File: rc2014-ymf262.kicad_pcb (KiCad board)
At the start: 2 copper layers, 100 x 50 mm, 19 parts, among them CON1 SJ1-3523N, P1 RC2014 BUS, U1 74HCT688, U2 YM3812, U3 YM3014B, U4 LM358, X1 3.579545MHz

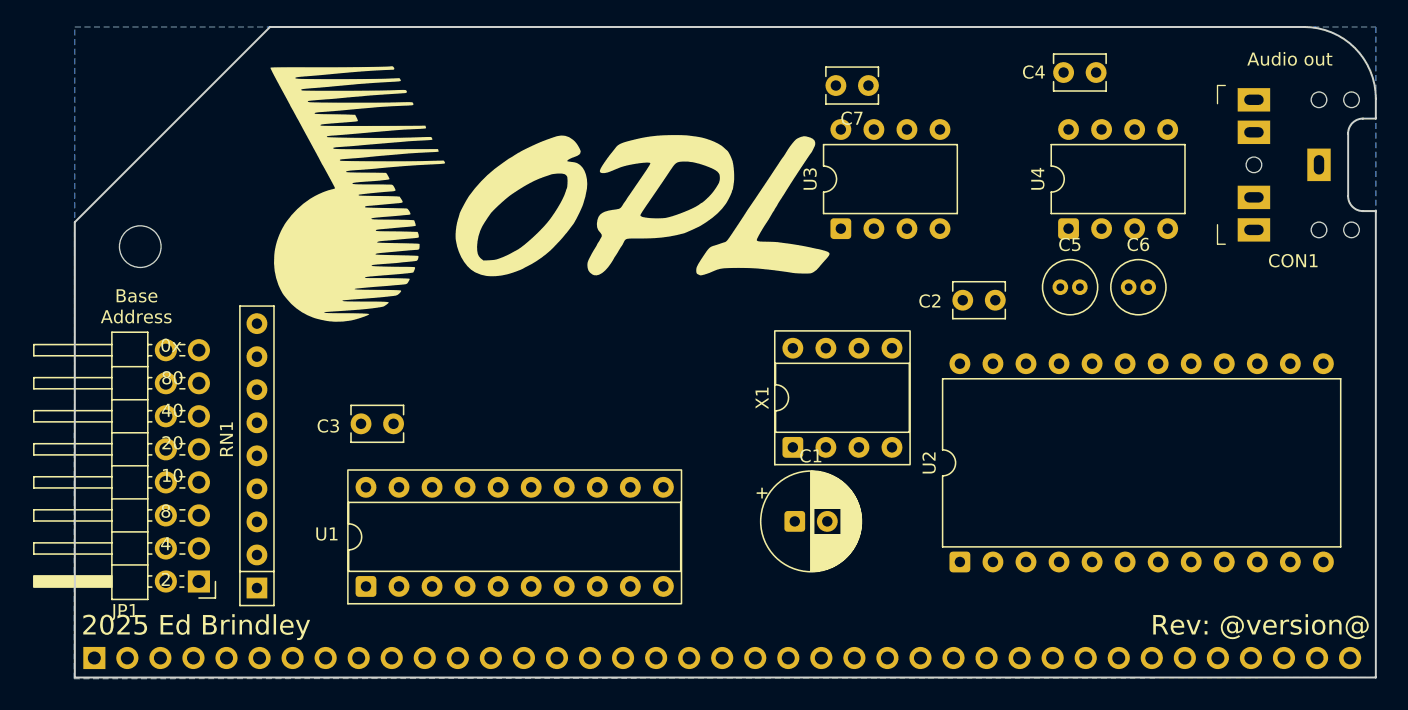
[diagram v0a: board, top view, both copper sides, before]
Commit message: move to use mostly SMD
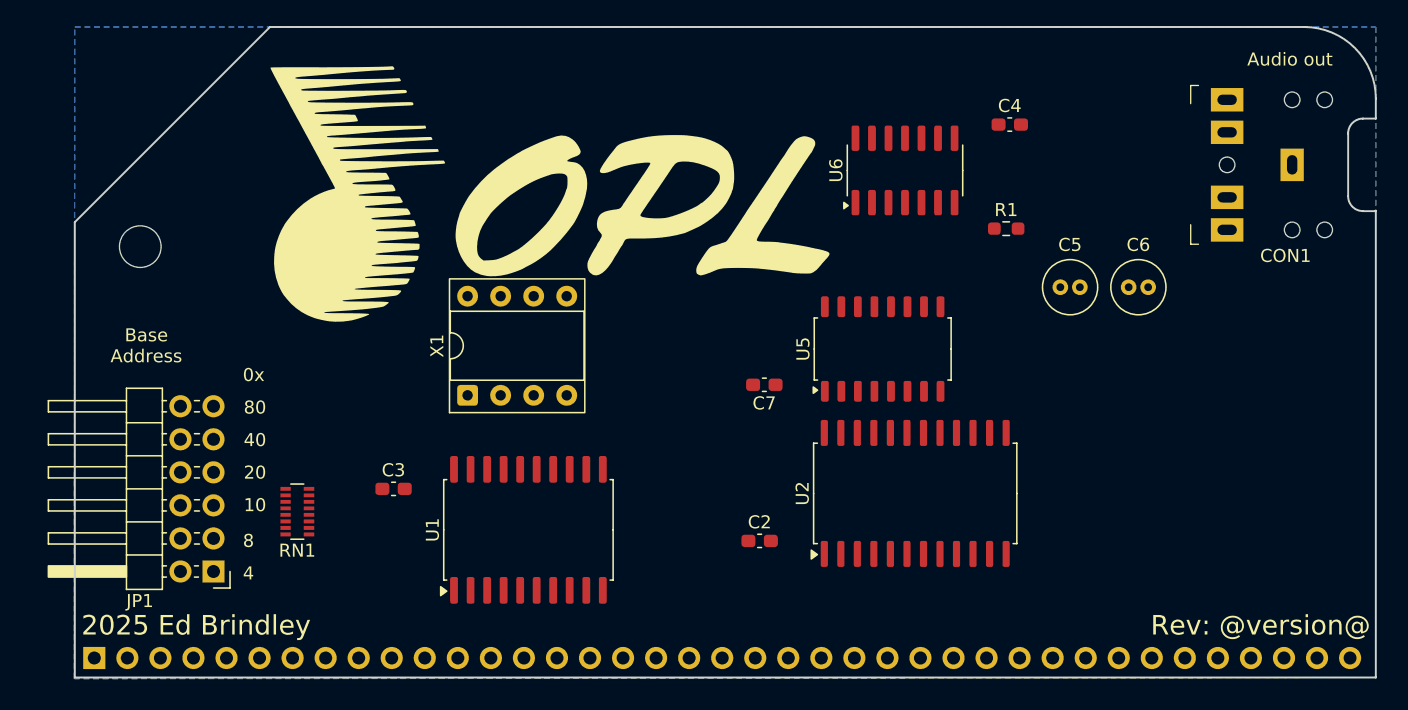
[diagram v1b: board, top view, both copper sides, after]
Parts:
- removed C1: 4.7uF, Capacitor_THT:CP_Radial_D7.5mm_P2.50mm
- removed U3: YM3014B, Package_DIP:DIP-8_W7.62mm
- removed U4: LM358, Package_DIP:DIP-8_W7.62mm
- added R1: R, Resistor_SMD:R_0603_1608Metric_Pad0.98x0.95mm_HandSolder, F.Cu at (132.1, 130.0)
- added U5: YAC512, Package_SO:SOP-16_4.55x10.3mm_P1.27mm, F.Cu at (122.6, 139.2)
- added U6: TL074, Package_SO:SOIC-14_3.9x8.7mm_P1.27mm, F.Cu at (124.3, 125.5)
- C2, C3, C4, C7: footprint Capacitor_THT:C_Disc_D3.8mm_W2.6mm_P2.50mm -> Capacitor_SMD:C_0603_1608Metric_Pad1.08x0.95mm_HandSolder
- JP1: footprint Connector_PinHeader_2.54mm:PinHeader_2x08_P2.54mm_Horizontal -> Connector_PinHeader_2.54mm:PinHeader_2x06_P2.54mm_Horizontal
- RN1: footprint Resistor_THT:R_Array_SIP9 -> Resistor_SMD:R_Array_Convex_8x0602
- U1: footprint Package_DIP:DIP-20_W7.62mm_Socket -> Package_SO:SOIC-20W_7.5x12.8mm_P1.27mm
- U2: value YM3812 -> YMF262; footprint Package_DIP:DIP-24_W15.24mm -> Package_SO:SOP-24_7.5x15.4mm_P1.27mm
- X1: value 3.579545MHz -> 14.318MHz
- moved X1 25.3 mm to (90.7, 142.8)
- moved C7 24.4 mm to (113.5, 142.0)
- moved C2 24.2 mm to (113.1, 154.0)
- moved U1 13.2 mm to (95.4, 153.2)
- moved RN1 6.64 mm to (77.6, 151.8), turned to 180 degrees
- moved U2 6.29 mm to (125.1, 150.3)
- moved C4 5.75 mm to (132.4, 122.0)
- moved C3 5.59 mm to (85.0, 150.0)
- moved CON1 2.06 mm to (149.1, 125.1)
- moved JP1 1.36 mm to (71.2, 156.3)
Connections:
- CON1 pad R: Net-(U4A--) -> /R
- CON1 pad RN: Net-(U4A--) -> /R
- CON1 pad T: Net-(U4A--) -> /L
- CON1 pad TN: Net-(U4A--) -> /L
- RN1 pad 8: Net-(JP1-Pin_14) -> (no net)
- RN1 pad 9: Net-(JP1-Pin_16) -> (no net)
- U1 pad 15: /A1 -> GND
- U1 pad 16: Net-(JP1-Pin_14) -> GND
- U2 pad 19: unconnected-(U2-NC-Pad19) -> /SMPBD
- U2 pad 20: /LOAD -> /SMPAC
- U2 pad 21: /SD -> /DOAB
- U2 pad 5: /~{WR} -> /A1
- U2 pad 6: /~{RD} -> /~{WR}
- U2 pad 7: /~{CS} -> /~{RD}
- U2 pad 8: unconnected-(U2-NC-Pad8) -> /~{CS}
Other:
- board text removed: "2"

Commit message: use custom oscillator footprint
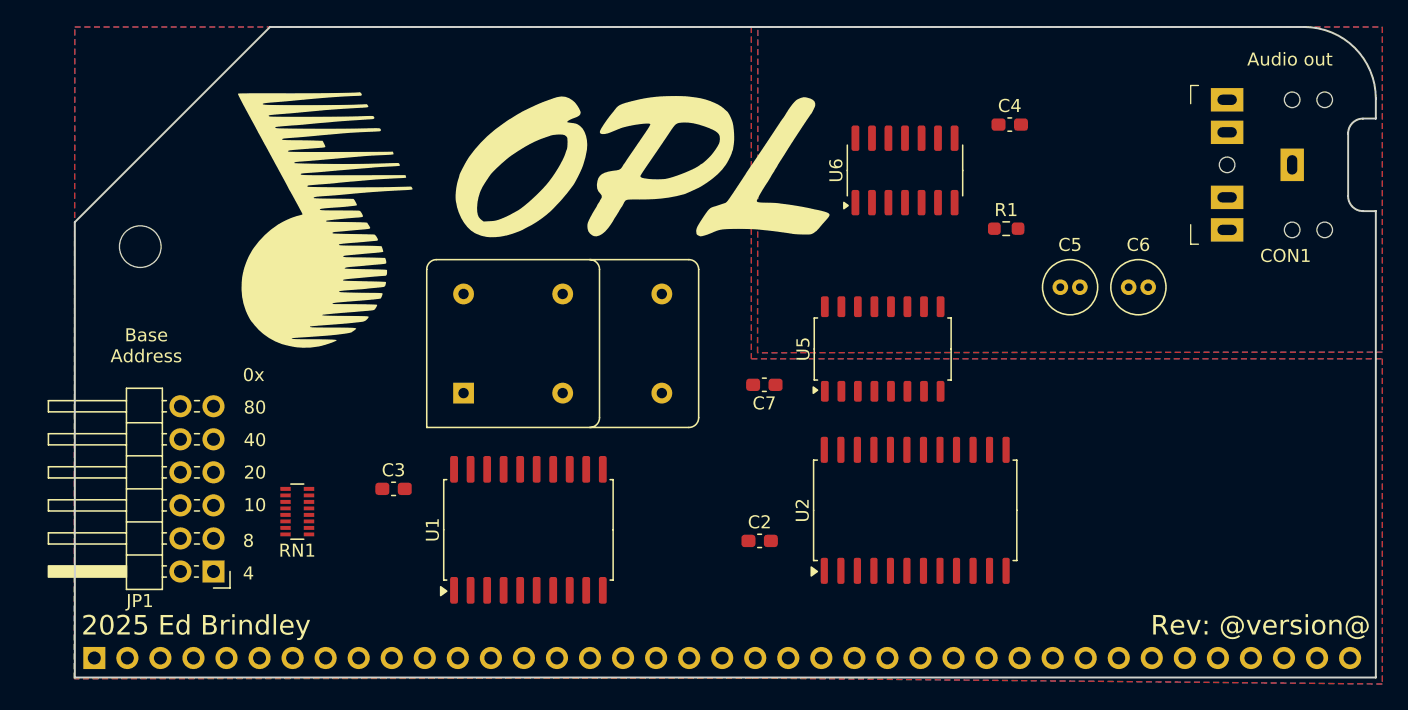
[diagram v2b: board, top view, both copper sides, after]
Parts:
- X1: footprint Package_DIP:DIP-8_W7.62mm_Socket -> electrified:Oscillator_DIP-8-14
- moved X1 8.24 mm to (98.0, 139.0), turned to 0 degrees
- moved G*** 3.20 mm to (79.0, 129.0)
- moved G*** 3.00 mm to (104.0, 125.0)
- moved U2 1.30 mm to (125.1, 151.7)
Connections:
- X1 pad 7: (no net) -> GND
- X1 pad 8: VCC -> /CLK
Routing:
- added copper zone on F.Cu, net GND
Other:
- board text added: "github.com/electrified/rc2014-ymf262"
- board text removed: "github.com/electrified/rc2014-ym3812"

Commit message: more work on schematic and layout
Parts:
- added C1: 10nF, Capacitor_SMD:C_0603_1608Metric_Pad1.08x0.95mm_HandSolder, F.Cu at (134.2, 137.0)
- added C10: 2.7nf, Capacitor_SMD:C_0603_1608Metric_Pad1.08x0.95mm_HandSolder, F.Cu at (114.1, 132.0)
- added C11: 2.7nf, Capacitor_SMD:C_0603_1608Metric_Pad1.08x0.95mm_HandSolder, F.Cu at (117.4, 118.5)
- added C12: 10uf, Capacitor_SMD:C_0603_1608Metric_Pad1.08x0.95mm_HandSolder, F.Cu at (132.9, 122.0)
- added C13: 10uF, Capacitor_SMD:C_1206_3216Metric, F.Cu at (155.8, 136.5)
- added C14: 10uf, Capacitor_SMD:C_0603_1608Metric_Pad1.08x0.95mm_HandSolder, F.Cu at (132.9, 128.0)
- added C15: 100nf, Capacitor_SMD:C_0603_1608Metric_Pad1.08x0.95mm_HandSolder, F.Cu at (129.1, 137.0)
- added C16: 470pF, Capacitor_SMD:C_0603_1608Metric_Pad1.08x0.95mm_HandSolder, F.Cu at (127.6, 123.0)
- added C17: 470pF, Capacitor_SMD:C_0603_1608Metric_Pad1.08x0.95mm_HandSolder, F.Cu at (112.1, 127.5)
- added C18: 3.9nF, Capacitor_SMD:C_0603_1608Metric_Pad1.08x0.95mm_HandSolder, F.Cu at (143.4, 122.0)
- added C19: 3.9nF, Capacitor_SMD:C_0603_1608Metric_Pad1.08x0.95mm_HandSolder, F.Cu at (143.1, 128.0)
- added C8: 100nF, Capacitor_SMD:C_0603_1608Metric_Pad1.08x0.95mm_HandSolder, F.Cu at (139.8, 137.0)
- added C9: 10uF, Capacitor_SMD:C_1206_3216Metric, F.Cu at (145.2, 137.0)
- added L1: BLM18PG221SN1D, Inductor_SMD:L_0603_1608Metric_Pad1.05x0.95mm_HandSolder, F.Cu at (136.9, 132.0)
- added L2: 33uH, Inductor_SMD:L_0603_1608Metric_Pad1.05x0.95mm_HandSolder, F.Cu at (150.8, 137.0)
- added R2: 15k, Resistor_SMD:R_0603_1608Metric_Pad0.98x0.95mm_HandSolder, F.Cu at (125.3, 118.5)
- added R3: 15k, Resistor_SMD:R_0603_1608Metric_Pad0.98x0.95mm_HandSolder, F.Cu at (112.2, 123.0)
- added R4: 1K, Resistor_SMD:R_0603_1608Metric_Pad0.98x0.95mm_HandSolder, F.Cu at (137.9, 122.0)
- added R5: 1K, Resistor_SMD:R_0603_1608Metric_Pad0.98x0.95mm_HandSolder, F.Cu at (137.9, 128.0)
- C5: value 10uF -> 68pf; footprint Capacitor_THT:C_Radial_D4.0mm_H7.0mm_P1.50mm -> Capacitor_SMD:C_0603_1608Metric_Pad1.08x0.95mm_HandSolder
- C6: footprint Capacitor_THT:C_Radial_D4.0mm_H7.0mm_P1.50mm -> Capacitor_SMD:C_0603_1608Metric_Pad1.08x0.95mm_HandSolder
- JP1: footprint Connector_PinHeader_2.54mm:PinHeader_2x06_P2.54mm_Horizontal -> Connector_PinHeader_2.54mm:PinHeader_2x06_P2.54mm_Vertical
- R1: value R -> 33
- moved C6 32.4 mm to (113.3, 118.5)
- moved C4 30.5 mm to (113.5, 146.0), turned to 180 degrees
- moved C5 21.9 mm to (121.3, 118.5)
- moved C7 11.0 mm to (118.1, 132.0)
- moved R1 9.04 mm to (123.3, 132.0)
- moved C2 8.99 mm to (122.0, 155.5), turned to 180 degrees
- moved U2 7.43 mm to (132.5, 151.0)
- moved G2 6.50 mm to (98.0, 122.5)
- moved U6 5.17 mm to (119.1, 125.5)
- moved X1 4.86 mm to (93.4, 137.5)
- moved JP1 4.66 mm to (66.5, 156.2)
- moved RN1 4.54 mm to (75.8, 147.6), turned to 90 degrees
- moved U5 3.67 mm to (119.0, 140.0)
- moved G1 2.75 mm to (76.3, 129.2)
- moved C3 2.50 mm to (83.0, 148.5)
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- renumbered G*** to G1, G*** to G2
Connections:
- C4 pad 1: VCC -> +5VA
- C7 pad 1: VCC -> +5VA
- CON1 pad R: /R -> Net-(C19-Pad1)
- CON1 pad RN: /R -> Net-(C19-Pad1)
- CON1 pad T: /L -> Net-(C18-Pad1)
- CON1 pad TN: /L -> Net-(C18-Pad1)
- JP1 pad 1: VCC -> Net-(JP1-Pin_1)
- JP1 pad 10: Net-(JP1-Pin_10) -> VCC
- JP1 pad 11: VCC -> Net-(JP1-Pin_11)
- JP1 pad 12: Net-(JP1-Pin_12) -> VCC
- JP1 pad 2: Net-(JP1-Pin_2) -> VCC
- JP1 pad 3: VCC -> Net-(JP1-Pin_3)
- JP1 pad 4: Net-(JP1-Pin_4) -> VCC
- JP1 pad 5: VCC -> Net-(JP1-Pin_5)
- JP1 pad 6: Net-(JP1-Pin_6) -> VCC
- JP1 pad 7: VCC -> Net-(JP1-Pin_7)
- JP1 pad 8: Net-(JP1-Pin_8) -> VCC
- JP1 pad 9: VCC -> Net-(JP1-Pin_9)
- RN1 pad 2: Net-(JP1-Pin_2) -> Net-(JP1-Pin_11)
- RN1 pad 3: Net-(JP1-Pin_4) -> Net-(JP1-Pin_9)
- RN1 pad 4: Net-(JP1-Pin_6) -> Net-(JP1-Pin_7)
- RN1 pad 5: Net-(JP1-Pin_8) -> Net-(JP1-Pin_5)
- RN1 pad 6: Net-(JP1-Pin_10) -> Net-(JP1-Pin_3)
- RN1 pad 7: Net-(JP1-Pin_12) -> Net-(JP1-Pin_1)
- U1 pad 12: Net-(JP1-Pin_10) -> Net-(JP1-Pin_3)
- U1 pad 14: Net-(JP1-Pin_12) -> Net-(JP1-Pin_1)
- U1 pad 3: Net-(JP1-Pin_2) -> Net-(JP1-Pin_11)
- U1 pad 5: Net-(JP1-Pin_4) -> Net-(JP1-Pin_9)
- U1 pad 7: Net-(JP1-Pin_6) -> Net-(JP1-Pin_7)
- U1 pad 9: Net-(JP1-Pin_8) -> Net-(JP1-Pin_5)
- U2 pad 2: /~{INT} -> unconnected-(U2-~{IRQ}-Pad2)
- U5 pad 1: VCC -> +5VA
- U5 pad 3: VCC -> +5VA
- U5 pad 6: GND -> +5VA
- U5 pad 9: GND -> +5VA
- U6 pad 13: /R -> Net-(U6D--)
- U6 pad 4: VCC -> +5VA
- U6 pad 9: /L -> Net-(U6C--)
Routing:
- net /A7: track 0.00 -> 10.1 mm
- net /A4: track 0.00 -> 10.1 mm
- net /A6: track 0.00 -> 10.1 mm
- net /A5: track 0.00 -> 9.93 mm
- net Net-(JP1-Pin_11): track 0.00 -> 7.13 mm
- net Net-(JP1-Pin_1): track 0.00 -> 6.75 mm
- net Net-(JP1-Pin_9): track 0.00 -> 5.24 mm
- net Net-(JP1-Pin_3): track 0.00 -> 4.79 mm
- net Net-(JP1-Pin_7): track 0.00 -> 4.10 mm
- net Net-(JP1-Pin_5): track 0.00 -> 3.94 mm

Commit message: add additional docs and other random updates
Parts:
- added REF**: ESD-Logo_6.6x6mm_SilkScreen, Symbol:ESD-Logo_6.6x6mm_SilkScreen, F.Cu at (147.5, 143.0)
- added REF**: WEEE-Logo_5.6x8mm_SilkScreen, Symbol:WEEE-Logo_5.6x8mm_SilkScreen, F.Cu at (157.0, 145.5)
- added REF**: WEEE-Logo_4.2x6mm_SilkScreen, Symbol:WEEE-Logo_4.2x6mm_SilkScreen, F.Cu at (146.0, 151.0)
- added REF**: OSHW-Symbol_6.7x6mm_SilkScreen, Symbol:OSHW-Symbol_6.7x6mm_SilkScreen, F.Cu at (152.5, 150.5)
- moved C10 14.3 mm to (127.5, 127.0)
- moved C6 13.4 mm to (118.0, 131.0)
- moved C18 1.35 mm to (142.5, 121.0), turned to 90 degrees
- moved R4 1.09 mm to (137.9, 120.9), turned to -90 degrees
- moved C7 1.01 mm to (118.0, 133.0)
- moved C12 1.01 mm to (133.0, 121.0), turned to 90 degrees
- turned C14 to 90 degrees
- turned C16 to 180 degrees
- turned C17 to 180 degrees
- turned C19 to 90 degrees
- turned L1 to 180 degrees
- turned R3 to 180 degrees
- turned R5 to -90 degrees
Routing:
- net VCC: track 0.00 -> 86.1 mm
- net /~{CS}: track 0.00 -> 48.9 mm, vias 0 -> 2
- net /CLK: track 0.00 -> 43.8 mm
- net /~{IORQ}: track 0.00 -> 42.8 mm, vias 0 -> 2
- net +5VA: track 0.00 -> 40.4 mm, vias 0 -> 5
- net /A1: track 0.00 -> 37.1 mm, vias 0 -> 2
- net /A0: track 0.00 -> 33.2 mm, vias 0 -> 2
- net /D7: track 0.00 -> 32.7 mm
- net /R: track 0.00 -> 32.4 mm, vias 0 -> 2
- net /D6: track 0.00 -> 29.3 mm
- net /D5: track 0.00 -> 27.1 mm
- net /A2: track 0.00 -> 26.8 mm
- net Net-(U5-CH1): track 0.00 -> 25.6 mm, vias 0 -> 2
- net /D4: track 0.00 -> 25.3 mm
- net /D3: track 0.00 -> 23.5 mm
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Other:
- board text added: "Default address 0x90"
